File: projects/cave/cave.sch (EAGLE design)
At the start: 111 parts, among them U1 IRLML6344TRPBF, U10 IRLML6344TRPBF, U11 IRLML6344TRPBF, U12 IRLML6344TRPBF, U2 TLC555CDR, U3 IRLML6344TRPBF, U4 IRLML6344TRPBF, U5 IRLML6344TRPBF, U6 IRLML6344TRPBF, U7 TPS54625, U9 IRLML6344TRPBF

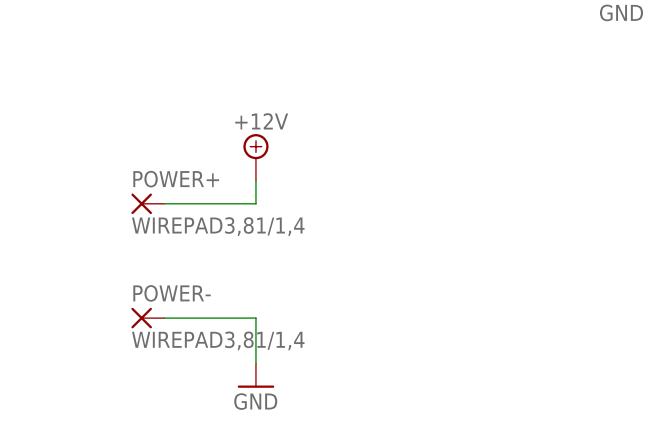
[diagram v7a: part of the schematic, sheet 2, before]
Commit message: Routing in progress... Added "Routing_prefs" script in lib folder to set custom default values and shortcuts. To run it, add "eagle_libs" folder as a script directory in eagle, and add "SCRIPT Routing_prefs.scr;" after "BRD:" in the "eagle.scr" script (located at $EAGLEDIR/scr)
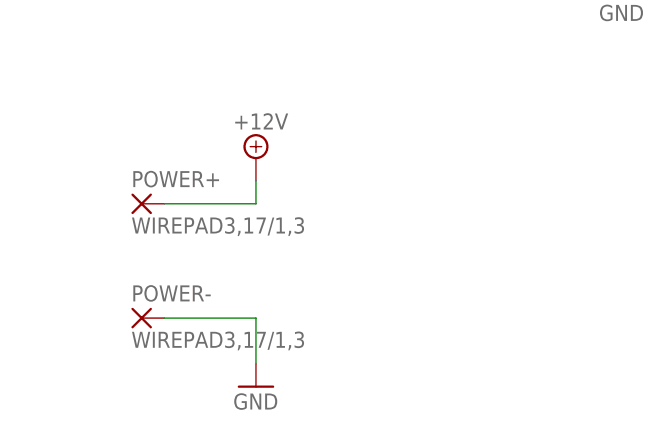
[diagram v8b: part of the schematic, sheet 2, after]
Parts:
- POWER+, POWER-: value WIREPAD3,81/1,4 -> WIREPAD3,17/1,3; device wirepad:WIREPAD3,81/1,4 -> wirepad:WIREPAD3,17/1,3
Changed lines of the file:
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@@
 <grid distance="0.1" unitdist="inch" unit="inch" style="lines" multiple="1" display="no" altdistance="0.01" altunitdist="inch" altunit="inch"/>
 <layers>
-<layer number="1" name="Top" color="4" fill="1" visible="no" active="no"/>
-<layer number="2" name="Route2" color="1" fill="3" visible="no" active="no"/>
-<layer number="3" name="Route3" color="4" fill="3" visible="no" active="no"/>
-<layer number="14" name="Route14" color="1" fill="6" visible="no" active="no"/>
-<layer number="15" name="Route15" color="4" fill="6" visible="no" active="no"/>
-<layer number="16" name="Bottom" color="1" fill="1" visible="no" active="no"/>
-<layer number="17" name="Pads" color="2" fill="1" visible="no" active="no"/>
-<layer number="18" name="Vias" color="2" fill="1" visible="no" active="no"/>
-<layer number="19" name="Unrouted" color="6" fill="1" visible="no" active="no"/>
-<layer number="20" name="Dimension" color="15" fill="1" visible="no" active="no"/>
-<layer number="21" name="tPlace" color="7" fill="1" visible="no" active="no"/>
-<layer number="22" name="bPlace" color="7" fill="1" visible="no" active="no"/>
-<layer number="23" name="tOrigins" color="15" fill="1" visible="no" active="no"/>
-<layer number="24" name="bOrigins" color="15" fill="1" visible="no" active="no"/>
-<layer number="25" name="tNames" color="7" fill="1" visible="no" active="no"/>
-<layer number="26" name="bNames" color="7" fill="1" visible="no" active="no"/>
-<layer number="27" name="tValues" color="7" fill="1" visible="no" active="no"/>
-<layer number="28" name="bValues" color="7" fill="1" visible="no" active="no"/>
+<layer number="1" name="Top" color="4" fill="1" visible="yes" active="no"/>
+<layer number="2" name="Route2" color="1" fill="3" visible="yes" active="no"/>
+<layer number="3" name="Route3" color="4" fill="3" visible="yes" active="no"/>
+<layer number="14" name="Route14" color="1" fill="6" visible="yes" active="no"/>
+<layer number="15" name="Route15" color="4" fill="6" visible="yes" active="no"/>
+<layer number="16" name="Bottom" color="1" fill="1" visible="yes" active="no"/>
+<layer number="17" name="Pads" color="2" fill="1" visible="yes" active="no"/>
+<layer number="18" name="Vias" color="2" fill="1" visible="yes" active="no"/>
+<layer number="19" name="Unrouted" color="6" fill="1" visible="yes" active="no"/>
+<layer number="20" name="Dimension" color="15" fill="1" visible="yes" active="no"/>
+<layer number="21" name="tPlace" color="7" fill="1" visible="yes" active="no"/>
+<layer number="22" name="bPlace" color="7" fill="1" visible="yes" active="no"/>
+<layer number="23" name="tOrigins" color="15" fill="1" visible="yes" active="no"/>
+<layer number="24" name="bOrigins" color="15" fill="1" visible="yes" active="no"/>
+<layer number="25" name="tNames" color="7" fill="1" visible="yes" active="no"/>
+<layer number="26" name="bNames" color="7" fill="1" visible="yes" active="no"/>
+<layer number="27" name="tValues" color="7" fill="1" visible="yes" active="no"/>
+<layer number="28" name="bValues" color="7" fill="1" visible="yes" active="no"/>
 <layer number="29" name="tStop" color="7" fill="3" visible="no" active="no"/>
 <layer number="30" name="bStop" color="7" fill="6" visible="no" active="no"/>
@@
 <layer number="35" name="tGlue" color="7" fill="4" visible="no" active="no"/>
 <layer number="36" name="bGlue" color="7" fill="5" visible="no" active="no"/>
-<layer number="37" name="tTest" color="7" fill="1" visible="no" active="no"/>
-<layer number="38" name="bTest" color="7" fill="1" visible="no" active="no"/>
+<layer number="37" name="tTest" color="7" fill="1" visible="yes" active="no"/>
+<layer number="38" name="bTest" color="7" fill="1" visible="yes" active="no"/>
 <layer number="39" name="tKeepout" color="4" fill="11" visible="no" active="no"/>
 <layer number="40" name="bKeepout" color="1" fill="11" visible="no" active="no"/>
@@
 <layer number="44" name="Drills" color="7" fill="1" visible="no" active="no"/>
 <layer number="45" name="Holes" color="7" fill="1" visible="no" active="no"/>
-<layer number="46" name="Milling" color="3" fill="1" visible="no" active="no"/>
-<layer number="47" name="Measures" color="7" fill="1" visible="no" active="no"/>
-<layer number="48" name="Document" color="7" fill="1" visible="no" active="no"/>
-<layer number="49" name="Reference" color="7" fill="1" visible="no" active="no"/>
-<layer number="50" name="dxf" color="7" fill="1" visible="no" active="no"/>
-<layer number="51" name="tDocu" color="7" fill="1" visible="no" active="no"/>
-<layer number="52" name="bDocu" color="7" fill="1" visible="no" active="no"/>
-<layer number="53" name="tGND_GNDA" color="7" fill="9" visible="no" active="no"/>
-<layer number="54" name="bGND_GNDA" color="1" fill="9" visible="no" active="no"/>
-<layer number="56" name="wert" color="7" fill="1" visible="no" active="no"/>
-<layer number="59" name="Invisible" color="7" fill="1" visible="no" active="no"/>
-<layer number="61" name="stand" color="7" fill="1" visible="no" active="no"/>
+<layer number="46" name="Milling" color="3" fill="1" visible="yes" active="no"/>
+<layer number="47" name="Measures" color="7" fill="1" visible="yes" active="no"/>
+<layer number="48" name="Document" color="7" fill="1" visible="yes" active="no"/>
+<layer number="49" name="Reference" color="7" fill="1" visible="yes" active="no"/>
+<layer number="50" name="dxf" color="7" fill="1" visible="yes" active="no"/>
+<layer number="51" name="tDocu" color="7" fill="1" visible="yes" active="no"/>
+<layer number="52" name="bDocu" color="7" fill="1" visible="yes" active="no"/>
+<layer number="53" name="tGND_GNDA" color="7" fill="9" visible="yes" active="no"/>
+<layer number="54" name="bGND_GNDA" color="1" fill="9" visible="yes" active="no"/>
+<layer number="56" name="wert" color="7" fill="1" visible="yes" active="no"/>
+<layer number="59" name="Invisible" color="7" fill="1" visible="yes" active="no"/>
+<layer number="61" name="stand" color="7" fill="1" visible="yes" active="no"/>
 <layer number="90" name="Modules" color="5" fill="1" visible="yes" active="yes"/>
 <layer number="91" name="Nets" color="2" fill="1" visible="yes" active="yes"/>
@@
 <part name="D-12V" library="rcl" deviceset="R-EU_" device="R0805" value="0"/>
 <part name="D-5V" library="rcl" deviceset="R-EU_" device="R0805" value="0"/>
-<part name="POWER+" library="wirepad" deviceset="WIREPAD" device="3,81/1,4"/>
-<part name="POWER-" library="wirepad" deviceset="WIREPAD" device="3,81/1,4"/>
+<part name="POWER+" library="wirepad" deviceset="WIREPAD" device="3,17/1,3" value="WIREPAD3,17/1,3"/>
+<part name="POWER-" library="wirepad" deviceset="WIREPAD" device="3,17/1,3" value="WIREPAD3,17/1,3"/>
 <part name="GND14" library="supply1" deviceset="GND" device=""/>
 <part name="SUPPLY1" library="supply2" deviceset="+12V" device=""/>
